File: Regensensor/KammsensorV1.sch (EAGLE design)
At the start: 19 parts

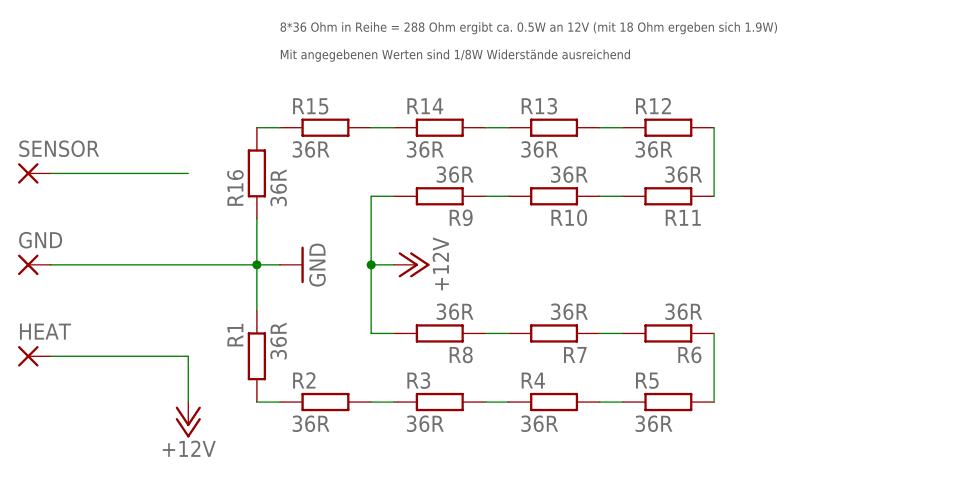
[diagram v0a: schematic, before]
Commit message: Add alternative drop detector
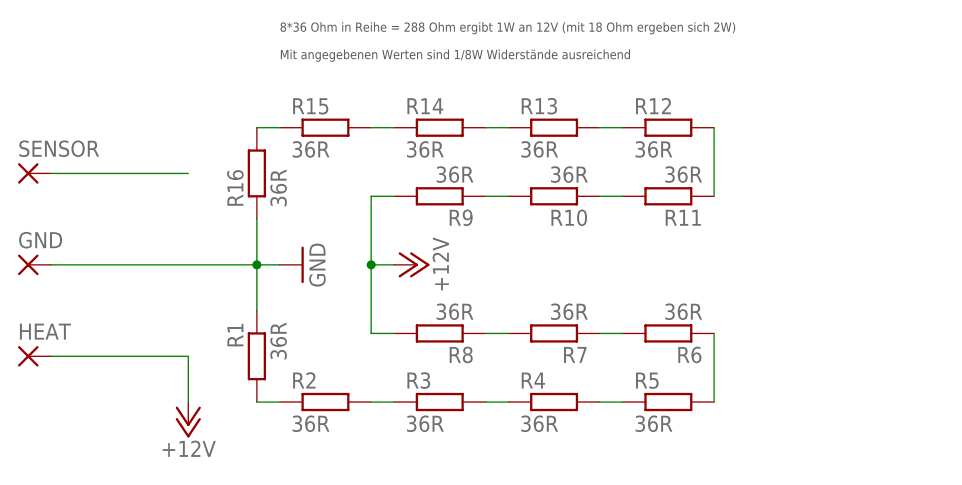
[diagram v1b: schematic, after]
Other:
- note added: "8*36 Ohm in Reihe = 288 Ohm ergibt 1W an 12V (mit 18 Ohm ergeben sich 2W) Mit angegebenen Werten sind 1/8W Widerstände ausreichend"
- note removed: "8*36 Ohm in Reihe = 288 Ohm ergibt ca. 0.5W an 12V (mit 18 Ohm ergeben sich 1.9W) Mit angegebenen Werten sind 1/8W Widerstände ausreichend"
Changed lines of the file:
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@@
 <sheet>
 <plain>
-<text x="182.88" y="127" size="1.016" layer="97">8*36 Ohm in Reihe = 288 Ohm ergibt ca. 0.5W an 12V (mit 18 Ohm ergeben sich 1.9W)
+<text x="182.88" y="127" size="1.016" layer="97">8*36 Ohm in Reihe = 288 Ohm ergibt 1W an 12V (mit 18 Ohm ergeben sich 2W)
 Mit angegebenen Werten sind 1/8W Widerstände ausreichend</text>
 </plain>
@@
 </busses>
 <nets>
-<net name="N$2" class="1">
+<net name="N$2" class="0">
 <segment>
 <pinref part="R2" gate="G$1" pin="2"/>
@@
 </segment>
 </net>
-<net name="N$7" class="1">
+<net name="N$7" class="0">
 <segment>
 <pinref part="R2" gate="G$1" pin="1"/>
